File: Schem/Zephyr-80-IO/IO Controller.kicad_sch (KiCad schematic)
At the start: 15 parts, among them IC1 Z80CTC, IC2 Z80SIO, IC3 Z80SIO, SW1 SW_Push, SW2 SW_Push, U1 ATmega1284-PU

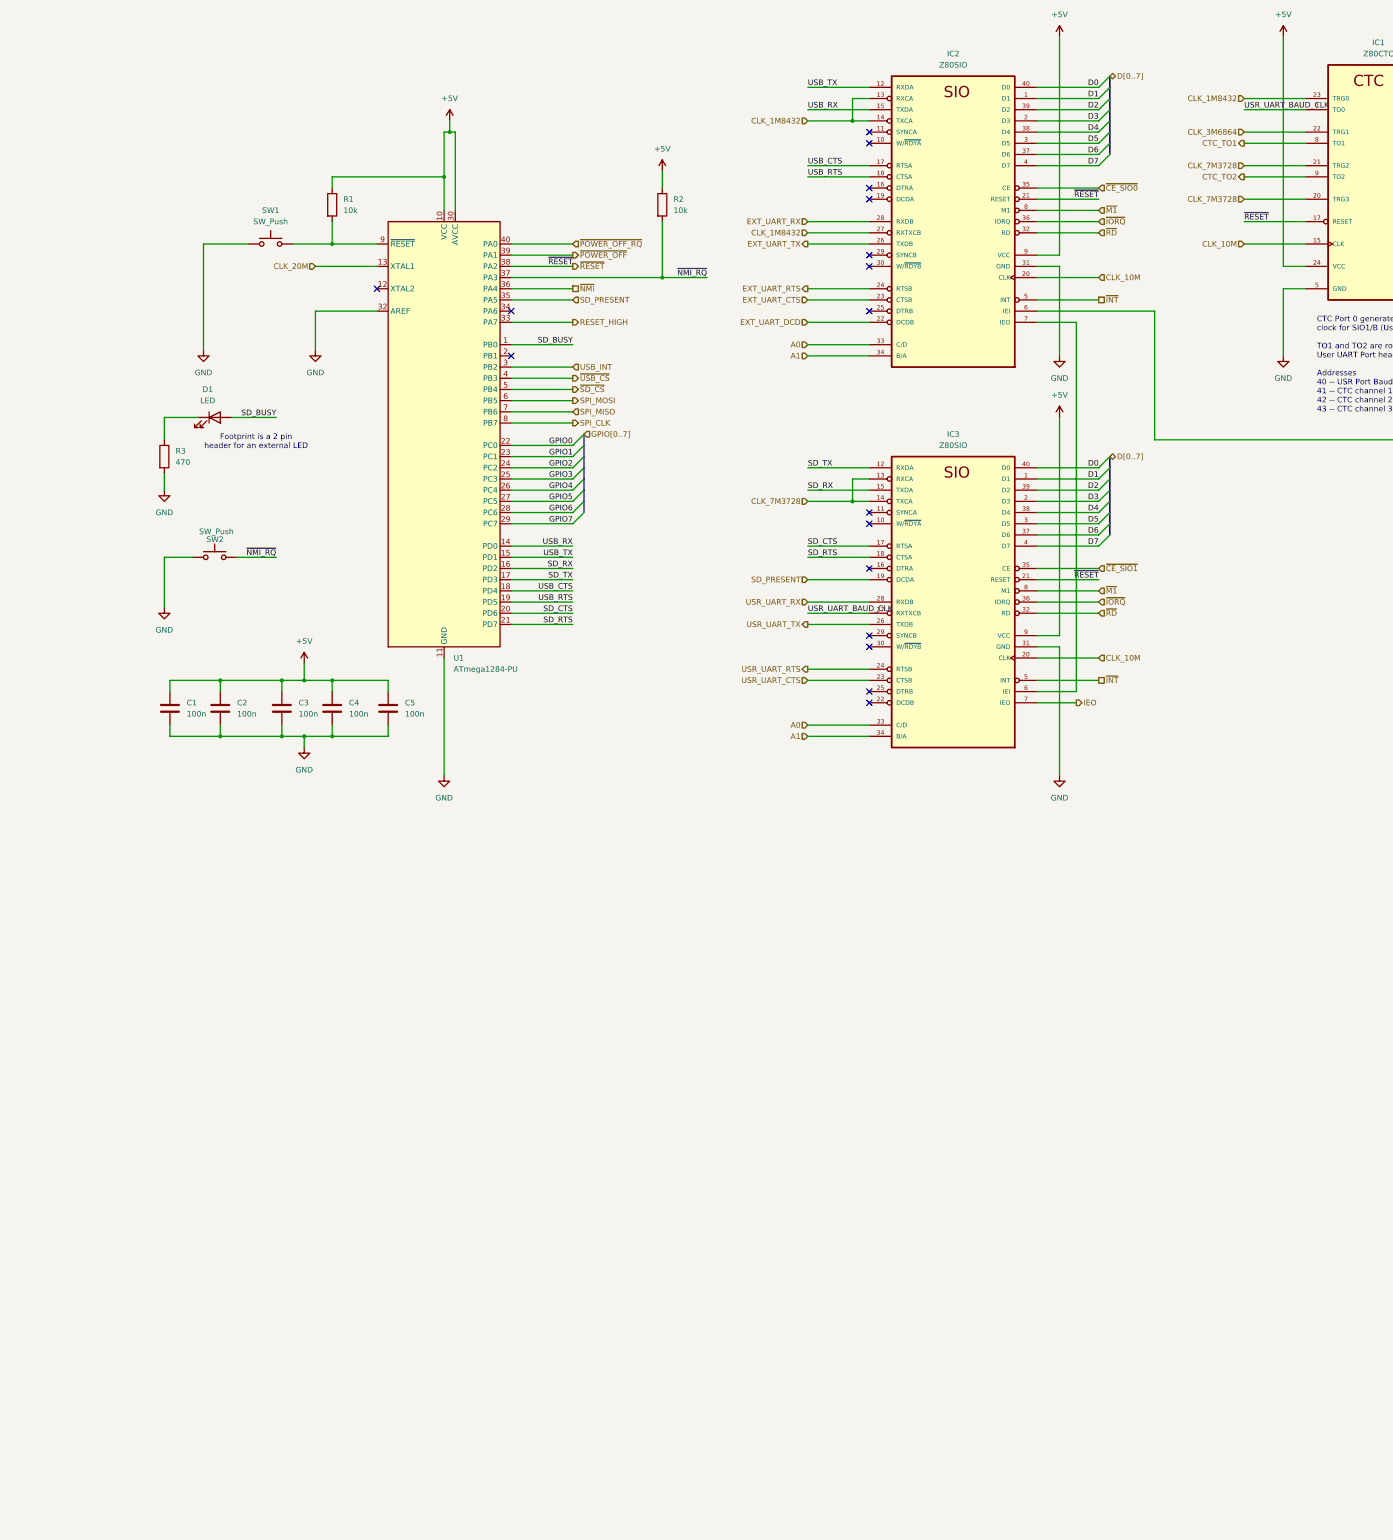
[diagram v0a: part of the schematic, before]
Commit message: Completed the IO Controller schematic and PCB layout for the Zephyr-80 project. This includes the design of the Baud Clock, CPU Address Decoding, Console Port, Device Select Decode, GPIO User Serial, and the main IO Controller schematics. Additionally, the PCB layout for the Zephyr-80 IO board has been created, along with the necessary library files and documentation for the control signal mapping.
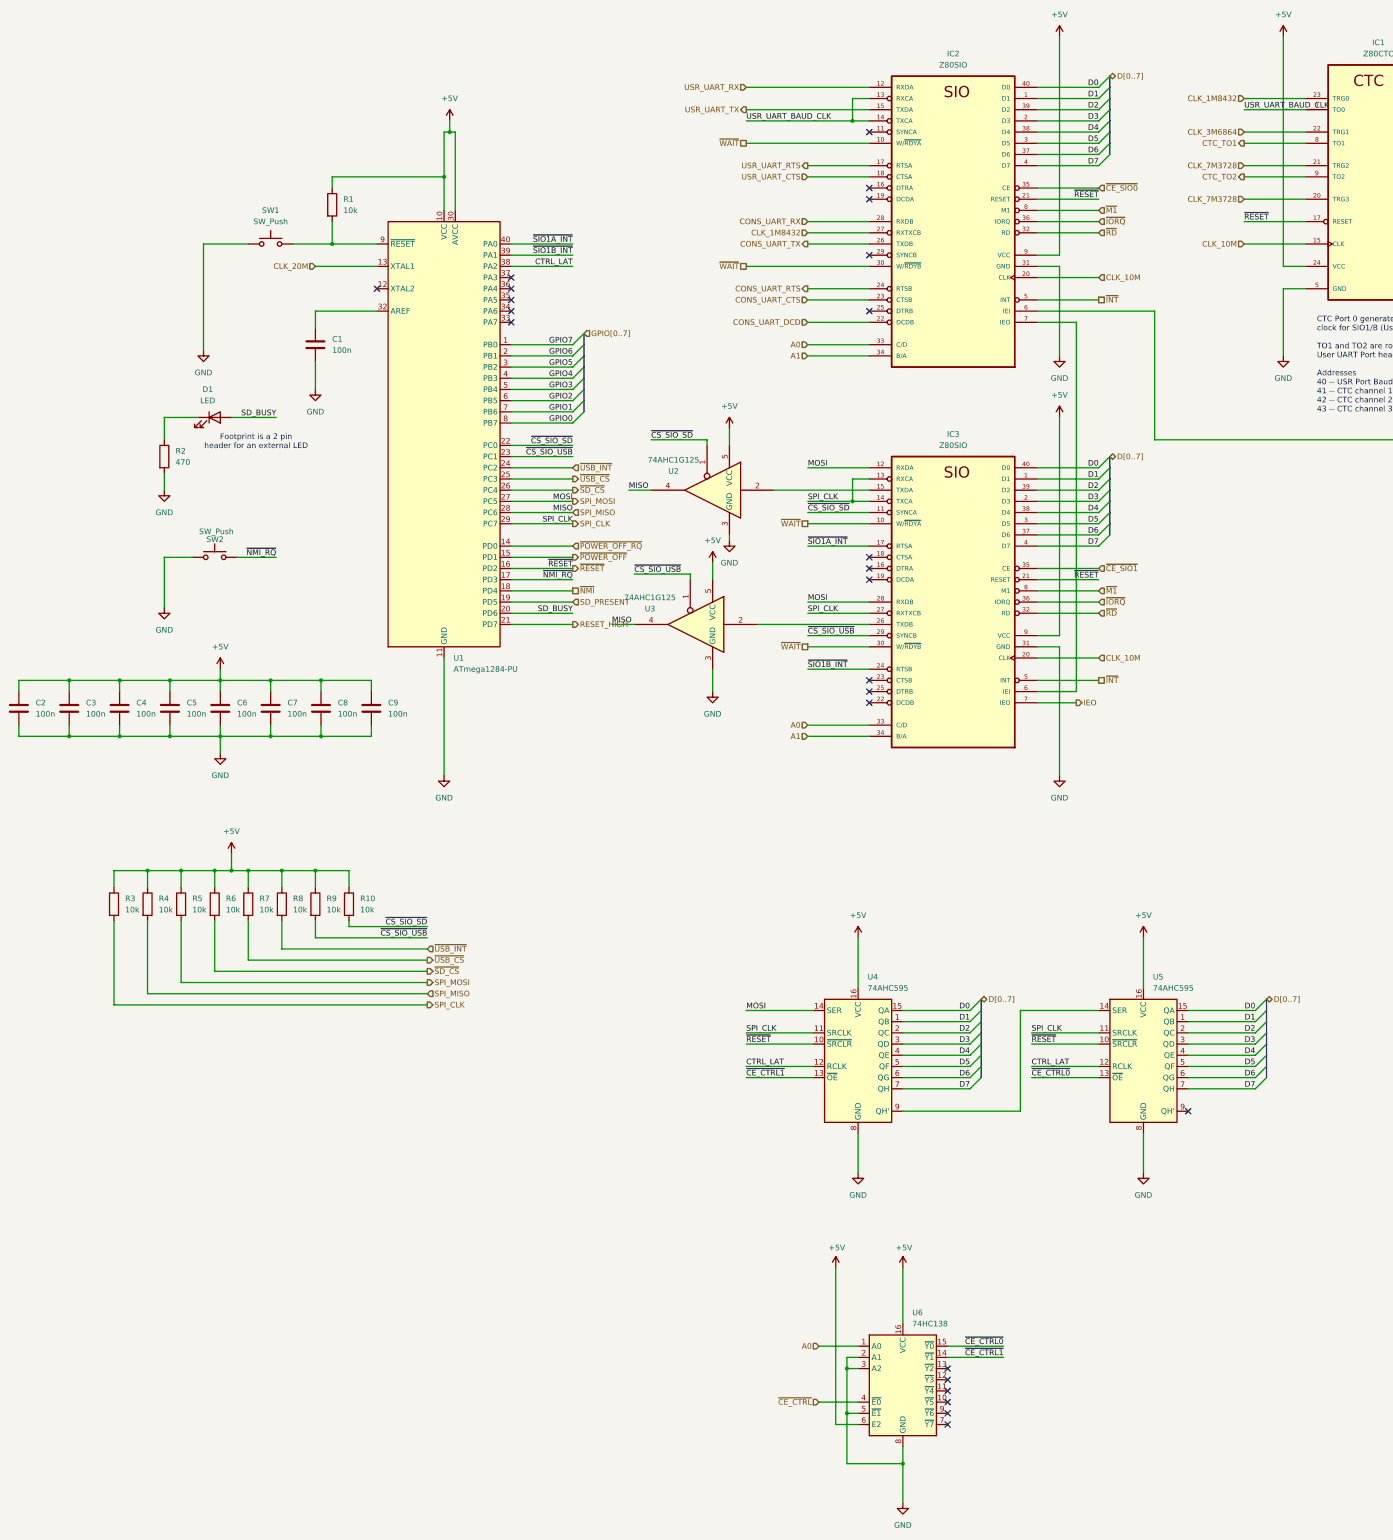
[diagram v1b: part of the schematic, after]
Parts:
- removed R2: 10k, Resistor_SMD:R_0603_1608Metric, symbol Device:R
- added C1, C2, C3, C4: 100n, Capacitor_SMD:C_0603_1608Metric, symbol Device:C
- added R10, R3, R4, R5, R6, R7, R8, R9: 10k, Resistor_SMD:R_0603_1608Metric, symbol Device:R
- added U2, U3: 74AHC1G125, Package_TO_SOT_SMD:SC-74A-5_1.55x2.9mm_P0.95mm, symbol 74xGxx:74AHC1G125
- added U4, U5: 74AHC595, Package_SO:TSSOP-16_4.4x5mm_P0.65mm, symbol 74xx:74AHC595
- added U6: 74HC138, Package_SO:TSSOP-16_4.4x5mm_P0.65mm, symbol 74xx:74HCT138
- U1: footprint Package_DIP:DIP-40_W15.24mm -> Package_DIP:DIP-40_W15.24mm_Socket
- renumbered C1 to C5, C2 to C6, C3 to C7, C4 to C8, C5 to C9, R3 to R2
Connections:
- net USB_INT is gone; now on net GPIO5: U1.3 (PB2)
- net +5V: now also C2.1, C3.1, C4.1, R10.1, R3.1, R4.1, R5.1, R6.1, R7.1, R8.1, R9.1, U2.5 (VCC), U3.5 (VCC), U4.16 (VCC), U5.16 (VCC), U6.16 (VCC), U6.6 (E2)
- net A0: now also U6.1 (A0)
- net CLK_1M8432: no longer IC2.13 (RXCA), IC2.14 (TXCA)
- net CLK_7M3728: no longer IC3.13 (RXCA), IC3.14 (TXCA)
- net D0: now also U4.15 (QA), U5.15 (QA)
- net D1: now also U4.1 (QB), U5.1 (QB)
- net D2: now also U4.2 (QC), U5.2 (QC)
- net D3: now also U4.3 (QD), U5.3 (QD)
- net D4: now also U4.4 (QE), U5.4 (QE)
- net D5: now also U4.5 (QF), U5.5 (QF)
- net D6: now also U4.6 (QG), U5.6 (QG)
- net D7: now also U4.7 (QH), U5.7 (QH)
- net GND: now also C1.2, C2.2, C3.2, C4.2, U2.3 (GND), U3.3 (GND), U4.8 (GND), U5.8 (GND), U6.2 (A1), U6.3 (A2), U6.5 (~{E1}), U6.8 (GND); no longer U1.32 (AREF)
- net GPIO0: now also U1.8 (PB7); no longer U1.22 (PC0)
- net GPIO1: now also U1.7 (PB6); no longer U1.23 (PC1)
- net GPIO2: now also U1.6 (PB5); no longer U1.24 (PC2)
- net GPIO3: now also U1.5 (PB4); no longer U1.25 (PC3)
- net GPIO4: now also U1.4 (PB3); no longer U1.26 (PC4)
- net GPIO5: no longer U1.27 (PC5)
- net GPIO6: now also U1.2 (PB1); no longer U1.28 (PC6)
- net GPIO7: now also U1.1 (PB0); no longer U1.29 (PC7)
- net RESET_HIGH: now also U1.21 (PD7); no longer U1.33 (PA7)
- net SD_BUSY: now also U1.20 (PD6); no longer U1.1 (PB0)
- net SD_PRESENT: now also U1.19 (PD5); no longer IC3.19 (DCDA), U1.35 (PA5)
- net SPI_CLK: now also IC3.13 (RXCA), IC3.14 (TXCA), IC3.27 (RXTXCB), U1.29 (PC7), R3.2, U4.11 (SRCLK), U5.11 (SRCLK); no longer U1.8 (PB7)
- net SPI_MISO: now also U1.28 (PC6), R4.2, U2.4, U3.4; no longer U1.7 (PB6)
- net SPI_MOSI: now also IC3.12 (RXDA), IC3.28 (RXDB), U1.27 (PC5), R5.2, U4.14 (SER); no longer U1.6 (PB5)
- net USR_UART_BAUD_CLK: now also IC2.13 (RXCA), IC2.14 (TXCA); no longer IC3.27 (RXTXCB)
- net USR_UART_CTS: now also IC2.18 (CTSA); no longer IC3.23 (CTSB)
- net USR_UART_RTS: now also IC2.17 (RTSA); no longer IC3.24 (RTSB)
- net USR_UART_RX: now also IC2.12 (RXDA); no longer IC3.28 (RXDB)
- net USR_UART_TX: now also IC2.15 (TXDA); no longer IC3.26 (TXDB)
- net ~{NMI_RQ}: now also U1.17 (PD3); no longer U1.37 (PA3)
- net ~{NMI}: now also U1.18 (PD4); no longer U1.36 (PA4)
- net ~{POWER_OFF_RQ}: now also U1.14 (PD0); no longer U1.40 (PA0)
- net ~{POWER_OFF}: now also U1.15 (PD1); no longer U1.39 (PA1)
- net ~{RESET}: now also U1.16 (PD2), U4.10 (~{SRCLR}), U5.10 (~{SRCLR}); no longer U1.38 (PA2)
- net ~{SD_CS}: now also U1.26 (PC4), R6.2; no longer U1.5 (PB4)
- net ~{USB_CS}: now also U1.25 (PC3), R7.2; no longer U1.4 (PB3)
- net ~{WAIT}: now reaches IC3.10 (W/~{RDYA})
- net ~{WAIT}: now also IC2.10 (W/~{RDYA}), IC2.30 (W/~{RDYB}), IC3.30 (W/~{RDYB})
- net ~{CS_SIO_SD}: now reaches IC3.11 (SYNCA)
- net ~{CS_SIO_SD}: now also U1.22 (PC0), R10.2, U2.1
- net ~{CS_SIO_USB}: now reaches IC3.29 (SYNCB)
- net ~{CS_SIO_USB}: now also U1.23 (PC1), R9.2, U3.1
- net EXT_UART_CTS renamed CONS_UART_CTS
- net EXT_UART_DCD renamed CONS_UART_DCD
- net EXT_UART_RTS renamed CONS_UART_RTS
- net EXT_UART_RX renamed CONS_UART_RX
- net EXT_UART_TX renamed CONS_UART_TX
- net SD_CTS renamed ~{SIO1A_INT}
- net ~{SIO1A_INT}: now also U1.40 (PA0); no longer U1.20 (PD6)
- net SD_RTS: no longer names the net of IC3.18 (CTSA)
- net SD_RTS: no longer U1.21 (PD7)
- net SD_RX: no longer names the net of IC3.15 (TXDA)
- net SD_RX: now also U2.2; no longer U1.16 (PD2)
- removed net SD_TX: IC3.12 (RXDA), U1.17 (PD3)
- removed net USB_CTS: IC2.17 (RTSA), U1.18 (PD4)
- removed net USB_RTS: IC2.18 (CTSA), U1.19 (PD5)
- removed net USB_RX: IC2.15 (TXDA), U1.14 (PD0)
- removed net USB_TX: IC2.12 (RXDA), U1.15 (PD1)
- new net: IC3.26 (TXDB), U3.2
- new net: C1.1, U1.32 (AREF)
- new net: U4.9 (QH'), U5.14 (SER)
- new net CTRL_LAT: U1.38 (PA2), U4.12 (RCLK), U5.12 (RCLK)
- new net ~{CE_CTRL0}: U5.13 (~{OE}), U6.15 (~{Y0})
- new net ~{CE_CTRL1}: U4.13 (~{OE}), U6.14 (~{Y1})
- new net ~{CE_CTRL}: U6.4 (~{E0})
- new net ~{SIO1B_INT}: IC3.24 (RTSB), U1.39 (PA1)
- new net ~{USB_INT}: R8.2, U1.24 (PC2)
- no-connect marks 17 -> 24
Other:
- moved on the sheet: C7, C8, C9

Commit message: Updated the IO Controller to use the PIC18F57Q84-I/PT instead of the AVR
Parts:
- removed C1: 100n, Capacitor_SMD:C_0603_1608Metric, symbol Device:C
- removed U1: ATmega1284-PU, Package_DIP:DIP-40_W15.24mm_Socket, symbol MCU_Microchip_ATmega:ATmega1284-P
- added J5: Conn_01x08_Pin, Connector_PinHeader_1.27mm:PinHeader_1x08_P1.27mm_Vertical, symbol Connector:Conn_01x08_Pin
- added U15: PIC18F57Q84-I/PT, Footprints:TQFP48_PT_MCH, symbol 2026-02-07_23-07-57:PIC18F57Q84-I_PT
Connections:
- net +5V: now also J5.2 (Pin_2), U15.30 (VDD), U15.7 (VDD)
- net CTRL_LAT: now also U15.36 (RF0)
- net GND: now also J5.3 (Pin_3), U15.31 (VSS), U15.6 (VSS)
- net GPIO0: now also U15.5 (RD7)
- net GPIO1: now also U15.4 (RD6)
- net GPIO2: now also U15.3 (RD5)
- net GPIO3: now also U15.2 (RD4)
- net GPIO4: now also U15.45 (RD3)
- net GPIO5: now also U15.44 (RD2)
- net GPIO6: now also U15.43 (RD1)
- net GPIO7: now also U15.42 (RD0)
- net RESET_HIGH: now also U15.17 (RB5)
- net SD_BUSY: now also U15.13 (RF5)
- net SD_PRESENT: now also U15.12 (RF4)
- net SPI_CLK: now also U15.32 (RA7)
- net SPI_MISO: now also U15.33 (RA6)
- net SPI_MOSI: now also U15.26 (RA5)
- net ~{CS_SIO_SD}: now also U15.21 (RA0)
- net ~{CS_SIO_USB}: now also U15.22 (RA1)
- net ~{NMI_RQ}: now also U15.11 (RB3)
- net ~{NMI}: now also U15.16 (RB4)
- net ~{POWER_OFF_RQ}: now also U15.8 (RB0)
- net ~{POWER_OFF}: now also U15.9 (RB1)
- net ~{RESET}: now also U15.10 (RB2)
- net ~{SD_CS}: now also U15.25 (RA4)
- net ~{SIO1A_INT}: now also U15.38 (RF2)
- net ~{SIO1B_INT}: now also U15.37 (RF1)
- net ~{USB_CS}: now also U15.24 (RA3)
- net ~{USB_INT}: now also U15.23 (RA2)
- net ~{MCLR}: now reaches R1.2, SW1.2
- net ~{MCLR}: now also J5.1 (Pin_1), U15.20 (VPP/*MCLR/RE3)
- new net: J5.5 (Pin_5), U15.18 (ICSPCLK/RB6)
- new net: J5.4 (Pin_4), U15.19 (ICSPDAT/RB7)
- no-connect marks 24 -> 35
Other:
- moved on the sheet: D1, IC1, IC2, IC3, R1, R2, SW1, SW2, U2, U3
